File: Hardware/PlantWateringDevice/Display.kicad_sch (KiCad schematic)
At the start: 28 parts, among them J3 Conn_01x03_Pin, U10 74HC595, U4 74LVC1G3157, U5 74HC595

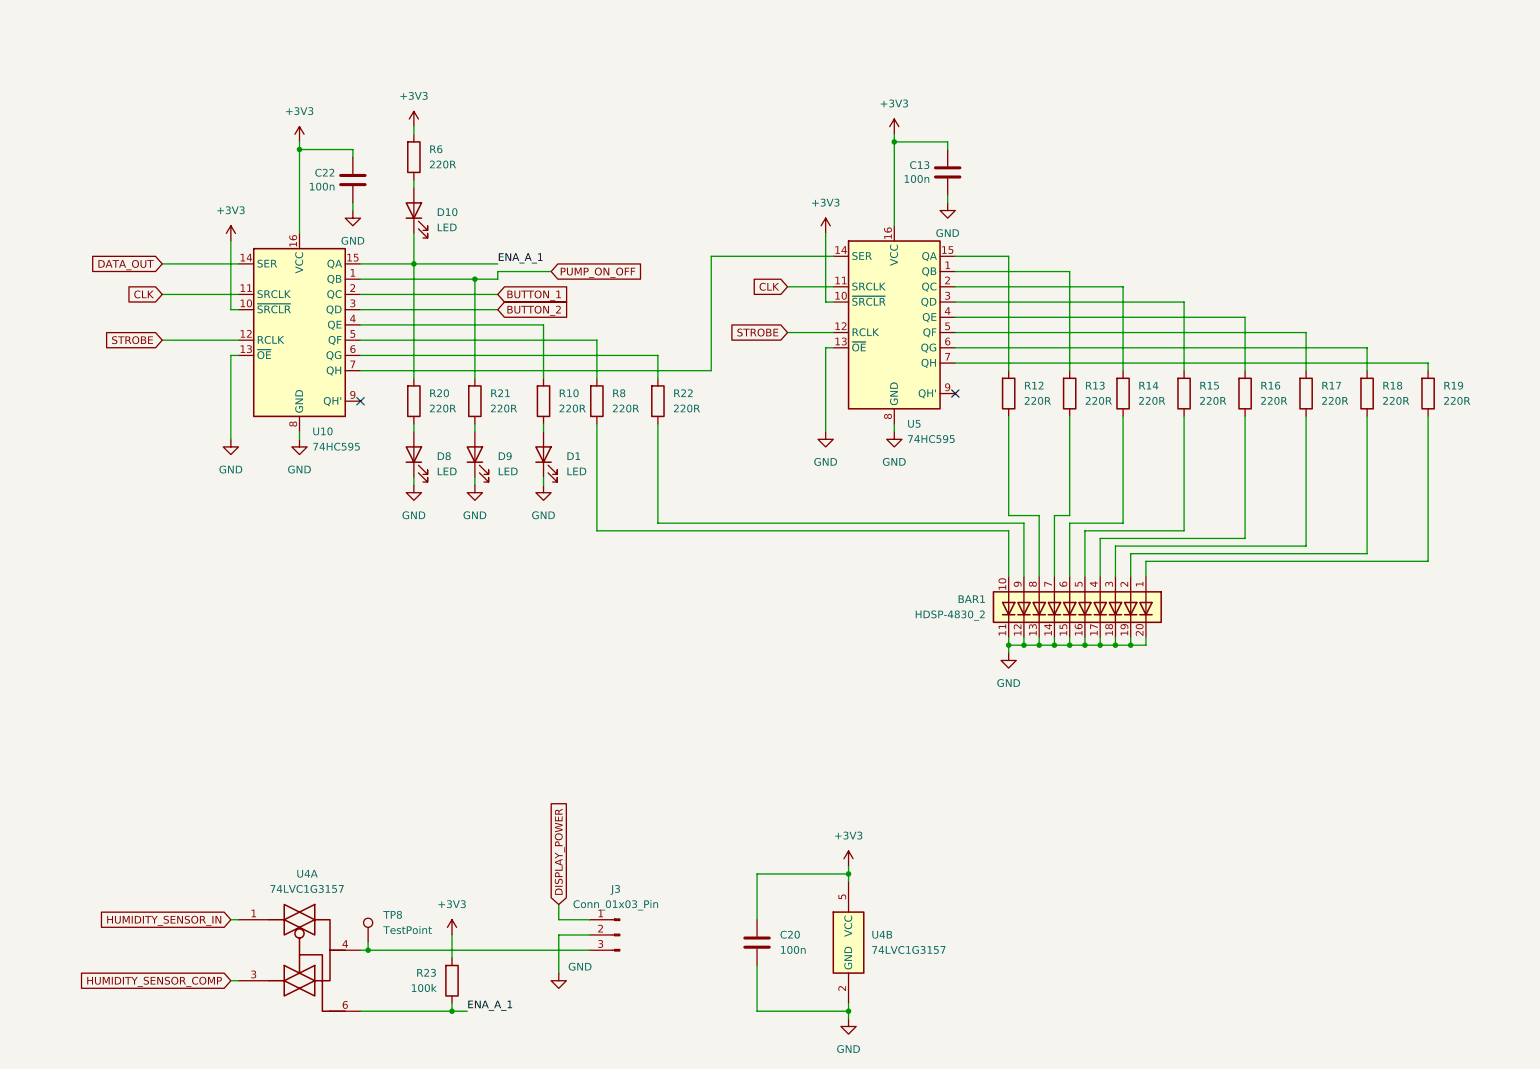
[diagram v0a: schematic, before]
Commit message: circuit simplification
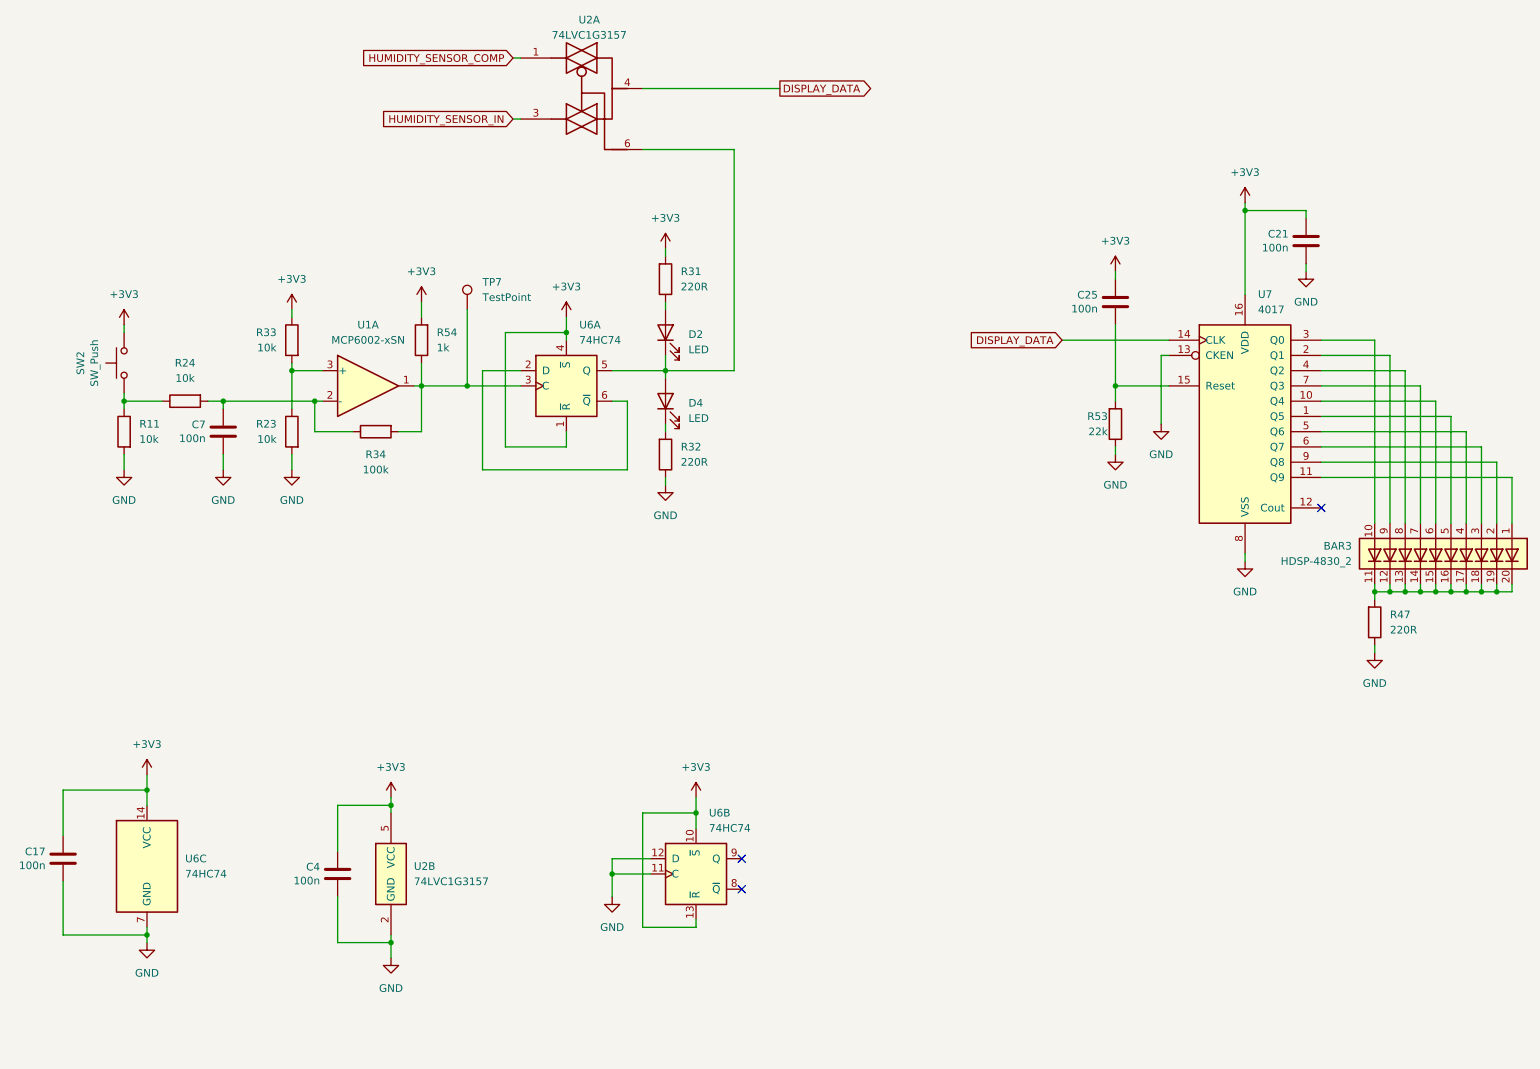
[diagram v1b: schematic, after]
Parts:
- removed BAR1: HDSP-4830_2, Display:HDSP-4830, symbol LED:HDSP-4830_2
- removed C13, C20, C22: 100n, Capacitor_SMD:C_0805_2012Metric, symbol Device:C
- removed D1, D10, D8, D9: LED, LED_THT:LED_D4.0mm, symbol Device:LED
- removed J3: Conn_01x03_Pin, Connector_PinHeader_2.54mm:PinHeader_1x03_P2.54mm_Vertical, symbol Connector:Conn_01x03_Pin
- removed R10, R12, R13, R14, R15, R16, R17, R18, R19, R20, R21, R22, R6, R8: 220R, Resistor_SMD:R_0805_2012Metric, symbol Device:R
- removed TP8: TestPoint, TestPoint:TestPoint_Pad_D2.0mm, symbol Connector:TestPoint
- removed U10, U5: 74HC595, Package_SO:SO-16_3.9x9.9mm_P1.27mm, symbol 74xx:74HC595
- removed U4: 74LVC1G3157, Package_TO_SOT_SMD:SOT-363_SC-70-6, symbol 74xGxx:74LVC1G3157
- added BAR3: HDSP-4830_2, Display:HDSP-4830, symbol LED:HDSP-4830_2
- added C17, C21, C25, C4, C7: 100n, Capacitor_SMD:C_0805_2012Metric, symbol Device:C
- added D2, D4: LED, LED_THT:LED_D4.0mm, symbol Device:LED
- added R11, R24, R33: 10k, Resistor_SMD:R_0805_2012Metric, symbol Device:R
- added R31, R32, R47: 220R, Resistor_SMD:R_0805_2012Metric, symbol Device:R
- added R34: 100k, Resistor_SMD:R_0805_2012Metric, symbol Device:R
- added R53: 22k, Resistor_SMD:R_0805_2012Metric, symbol Device:R
- added R54: 1k, Resistor_SMD:R_0805_2012Metric, symbol Device:R
- added SW2: SW_Push, Button_Switch_SMD:SW_SPST_PTS645, symbol Switch:SW_Push
- added TP7: TestPoint, TestPoint:TestPoint_Pad_D1.5mm, symbol Connector:TestPoint
- added U1: MCP6002-xSN, Package_SO:SO-8_3.9x4.9mm_P1.27mm, symbol Amplifier_Operational:MCP6002-xSN
- added U2: 74LVC1G3157, Package_TO_SOT_SMD:SOT-363_SC-70-6, symbol 74xGxx:74LVC1G3157
- added U6: 74HC74, Package_SO:SO-14_3.9x8.65mm_P1.27mm, symbol 74xx:74HC74
- added U7: 4017, Package_SO:SO-16_3.9x9.9mm_P1.27mm, symbol 4xxx:4017
- R23: value 100k -> 10k
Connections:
- net +3V3: now also C17.1, C21.1, C25.1, C4.1, R31.2, R33.1, R54.2, SW2.2, U2.5 (VCC), U6.1 (~{R}), U6.10 (~{S}), U6.13 (~{R}), U6.14 (VCC), U6.4 (~{S}), U7.16 (VDD); no longer R23.2
- net GND: now also R23.2, C17.2, C21.2, C4.2, C7.2, R11.2, R32.1, R47.1, R53.1, U2.2 (GND), U6.11 (C), U6.12 (D), U6.7 (GND), U7.13 (CKEN), U7.8 (VSS)
- net HUMIDITY_SENSOR_COMP: now also U2.1
- net HUMIDITY_SENSOR_IN: now also U2.3
- net ENA_A_1: no longer names the net of R23.1
- net ENA_A_1: now also R33.2, U1.3 (+)
- new net: C25.2, R53.2, U7.15 (Reset)
- new net: U6.2 (D), U6.6 (~{Q})
- new net: R34.2, R54.1, TP7.1, U1.1, U6.3 (C)
- new net: D2.1 (K), D4.2 (A), U2.6, U6.5 (Q)
- new net: C7.1, R24.2, R34.1, U1.2 (-)
- new net: R11.1, R24.1, SW2.1
- new net: BAR3.5 (A), U7.1 (Q5)
- new net: BAR3.6 (A), U7.10 (Q4)
- new net: BAR3.1 (A), U7.11 (Q9)
- new net: BAR3.9 (A), U7.2 (Q1)
- new net: BAR3.10 (A), U7.3 (Q0)
- new net: BAR3.8 (A), U7.4 (Q2)
- new net: BAR3.4 (A), U7.5 (Q6)
- new net: BAR3.3 (A), U7.6 (Q7)
- new net: BAR3.7 (A), U7.7 (Q3)
- new net: BAR3.2 (A), U7.9 (Q8)
- new net: D4.1 (K), R32.2
- new net: D2.2 (A), R31.1
- new net: BAR3.11 (K), BAR3.12 (K), BAR3.13 (K), BAR3.14 (K), BAR3.15 (K), BAR3.16 (K), BAR3.17 (K), BAR3.18 (K), BAR3.19 (K), BAR3.20 (K), R47.2
- new net DISPLAY_DATA: U2.4, U7.14 (CLK)
- no-connect marks 2 -> 3

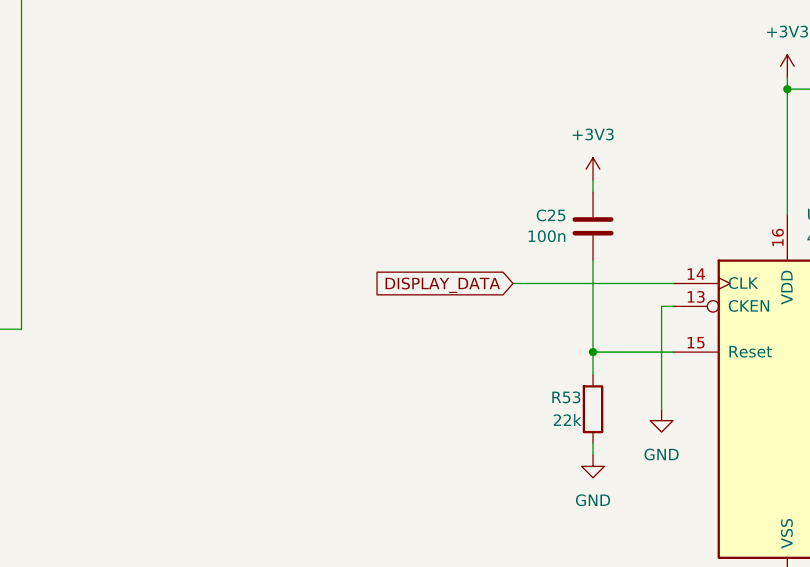
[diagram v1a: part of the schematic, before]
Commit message: use openscad for param modeling
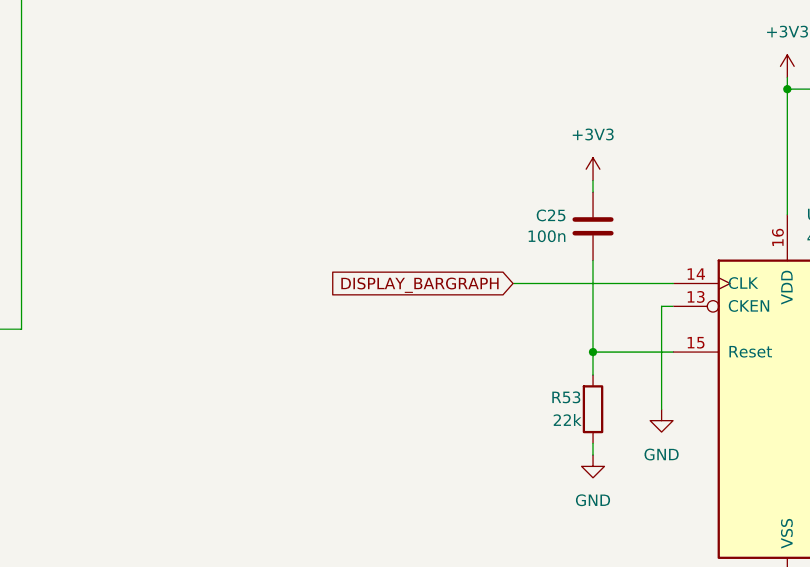
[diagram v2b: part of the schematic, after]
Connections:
- net DISPLAY_DATA: no longer U7.14 (CLK)
- new net DISPLAY_BARGRAPH: U7.14 (CLK)
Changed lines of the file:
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@@
 		)
 	)
-	(global_label "DISPLAY_DATA"
+	(global_label "DISPLAY_BARGRAPH"
 		(shape input)
 		(at 191.77 73.66 180)
@@
 		)
 		(property "Intersheetrefs" "${INTERSHEET_REFS}"
-			(at 175.8428 73.66 0)
+			(at 170.3999 73.66 0)
 			(effects
 				(font

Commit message: improvements after eric's comments
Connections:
- net +3V3 renamed VCC

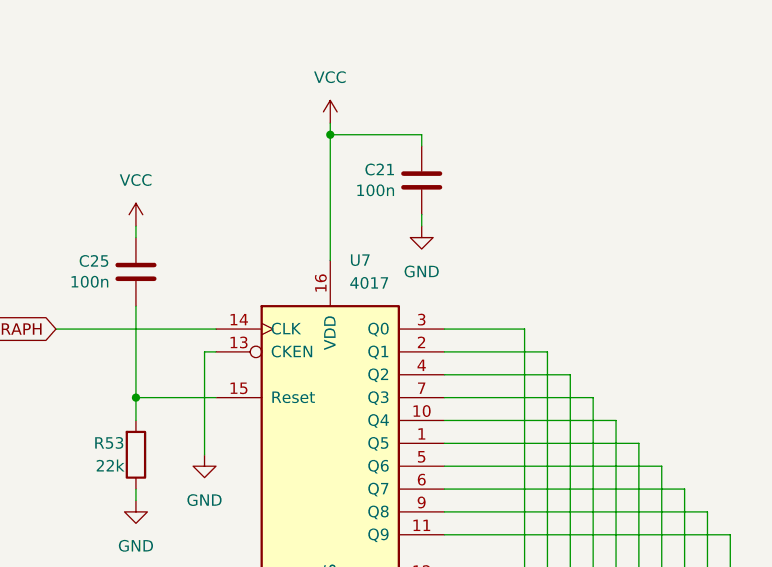
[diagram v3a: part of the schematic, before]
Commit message: fixes before sending pcb and 3d model to production
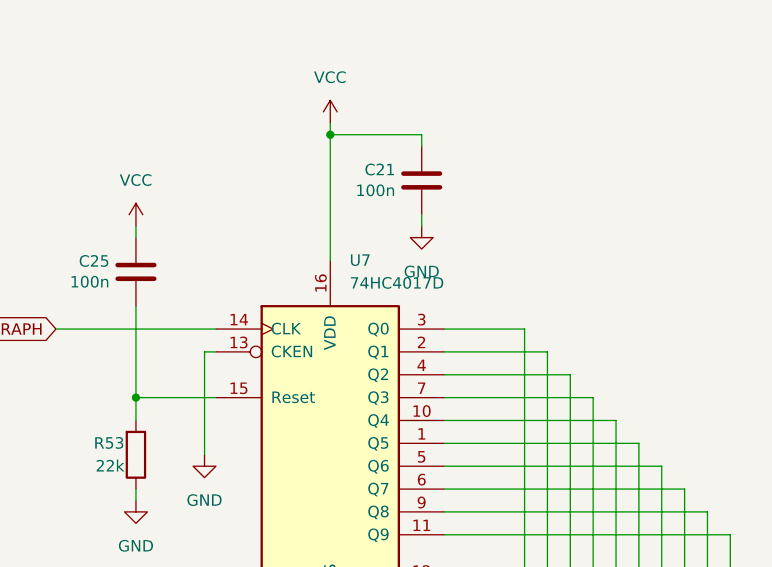
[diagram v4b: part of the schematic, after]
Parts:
- SW2: footprint Button_Switch_SMD:SW_SPST_PTS645 -> Button_Switch_SMD:SW_SPST_PTS645Sx43SMTR92
- U7: value 4017 -> 74HC4017D
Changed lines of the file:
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@@
 			)
 		)
-		(property "Footprint" "Button_Switch_SMD:SW_SPST_PTS645"
+		(property "Footprint" "Button_Switch_SMD:SW_SPST_PTS645Sx43SMTR92"
 			(at 30.48 77.47 0)
 			(effects
@@
 			)
 		)
-		(property "Value" "4017"
+		(property "Value" "74HC4017D"
 			(at 224.3933 68.58 0)
 			(effects

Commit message: firmware implementation
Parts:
- R31, R32, R47: value 220R -> 510R
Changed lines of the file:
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@@
 		(fields_autoplaced yes)
 		(property "Reference" "R32"
-			(at 128.27 91.4399 0)
-			(effects
-				(font
-					(size 1.27 1.27)
-				)
-				(justify left)
-			)
-		)
-		(property "Value" "220R"
-			(at 128.27 93.9799 0)
-			(effects
-				(font
-					(size 1.27 1.27)
-				)
-				(justify left)
+			(at 123.19 91.4399 0)
+			(effects
+				(font
+					(size 1.27 1.27)
+				)
+				(justify right)
+			)
+		)
+		(property "Value" "510R"
+			(at 123.19 93.9799 0)
+			(effects
+				(font
+					(size 1.27 1.27)
+				)
+				(justify right)
 			)
 		)
@@
 		(fields_autoplaced yes)
 		(property "Reference" "R31"
-			(at 128.27 62.2299 0)
-			(effects
-				(font
-					(size 1.27 1.27)
-				)
-				(justify left)
-			)
-		)
-		(property "Value" "220R"
-			(at 128.27 64.7699 0)
-			(effects
-				(font
-					(size 1.27 1.27)
-				)
-				(justify left)
+			(at 123.19 62.2299 0)
+			(effects
+				(font
+					(size 1.27 1.27)
+				)
+				(justify right)
+			)
+		)
+		(property "Value" "510R"
+			(at 123.19 64.7699 0)
+			(effects
+				(font
+					(size 1.27 1.27)
+				)
+				(justify right)
 			)
 		)
@@
 			)
 		)
-		(property "Value" "220R"
+		(property "Value" "510R"
 			(at 246.38 121.9199 0)
 			(effects
